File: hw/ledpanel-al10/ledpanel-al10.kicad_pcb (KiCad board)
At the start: 2 copper layers, 112.1 x 10.2 mm, 32 parts, among them J1 +5V, J2 DIN, J3 GND, J4 +5V, J5 DOUT, J6 GND

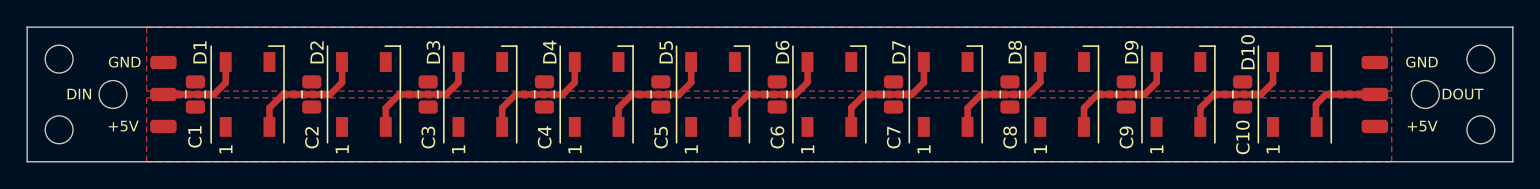
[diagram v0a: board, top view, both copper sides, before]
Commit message: hw - подвинуты отверстия din/dout на светодиодных лентах
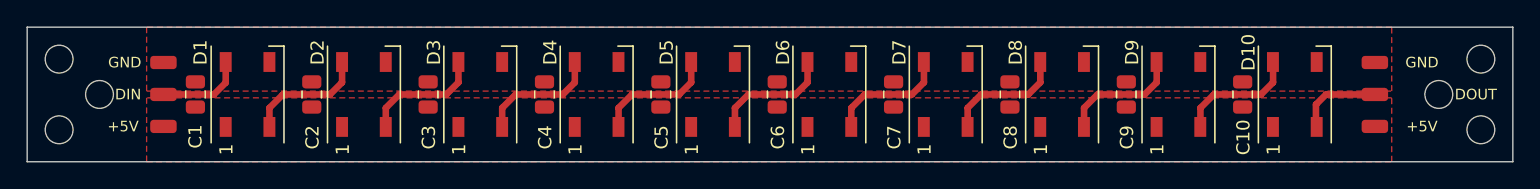
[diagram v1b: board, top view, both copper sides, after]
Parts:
- moved H3 1.02 mm to (30.9, 68.6)
- moved H6 1.02 mm to (132.0, 68.6)
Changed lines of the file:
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@@
         (effects (font (size 1 1) (thickness 0.15)))
     )
-    (fp_text value "DIN" (at 0 6.35) (layer "F.SilkS")
+    (fp_text value "DIN" (at 0 2.667) (layer "F.SilkS")
         (effects (font (size 0.8 0.8) (thickness 0.15)))
     )
@@
   )
   (footprint "MountingHole:MountingHole_2.1mm" (layer "F.Cu")
-    (at 130.937 68.58)
+    (at 131.953 68.58)
     (descr "Mounting Hole 2.1mm, no annular")
     (tags "mounting hole 2.1mm no annular")
@@
   )
   (footprint "MountingHole:MountingHole_2.1mm" (layer "F.Cu")
-    (at 31.877 68.58)
+    (at 30.861 68.58)
     (descr "Mounting Hole 2.1mm, no annular")
     (tags "mounting hole 2.1mm no annular")
@@
         (effects (font (size 1 1) (thickness 0.15)))
     )
-    (fp_text value "DOUT" (at 0 6.604 180) (layer "F.SilkS")
-        (effects (font (size 0.8 0.8) (thickness 0.15)))
-    )
+    (fp_text value "DOUT" (at 0 7.62 180) (layer "F.SilkS")
+        (effects (font (size 0.8 0.8) (thickness 0.15)))
+    )
